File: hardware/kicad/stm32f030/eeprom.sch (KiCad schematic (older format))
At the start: 1 part, among them IC1 AT24CS02-SSHM

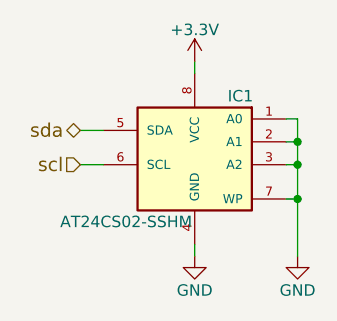
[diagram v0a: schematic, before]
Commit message: hardware/kicad/stm32f030: changed i2c bus and eeprom voltage to 5V
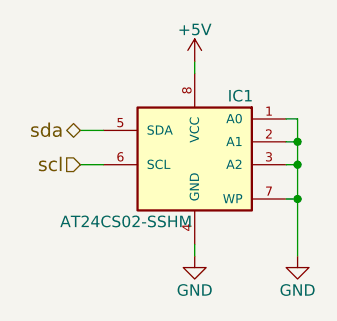
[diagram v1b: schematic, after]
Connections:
- net +3V3 renamed +5V
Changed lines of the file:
@@
 $EndComp
 $Comp
-L +3.3V #PWR045
-U 1 1 589C205E
-P 5600 2850
-F 0 "#PWR045" H 5600 2700 50  0001 C CNN
-F 1 "+3.3V" H 5600 2990 50  0000 C CNN
-F 2 "" H 5600 2850 50  0000 C CNN
-F 3 "" H 5600 2850 50  0000 C CNN
-	1    5600 2850
-	1    0    0    -1
-$EndComp
-$Comp
-L GND #PWR046
+L GND #PWR045
 U 1 1 589C2085
 P 5600 3700
-F 0 "#PWR046" H 5600 3450 50  0001 C CNN
+F 0 "#PWR045" H 5600 3450 50  0001 C CNN
 F 1 "GND" H 5600 3550 50  0000 C CNN
 F 2 "" H 5600 3700 50  0000 C CNN
@@
 	6050 3300 6000 3300
 $Comp
-L GND #PWR047
+L GND #PWR046
 U 1 1 589C239F
 P 6050 3700
-F 0 "#PWR047" H 6050 3450 50  0001 C CNN
+F 0 "#PWR046" H 6050 3450 50  0001 C CNN
 F 1 "GND" H 6050 3550 50  0000 C CNN
 F 2 "" H 6050 3700 50  0000 C CNN
@@
 Wire Wire Line
 	5600 2900 5600 2850
+$Comp
+L +5V #PWR047
+U 1 1 58BC2D81
+P 5600 2850
+F 0 "#PWR047" H 5600 2700 50  0001 C CNN
+F 1 "+5V" H 5600 2990 50  0000 C CNN
+F 2 "" H 5600 2850 50  0001 C CNN
+F 3 "" H 5600 2850 50  0001 C CNN
+	1    5600 2850
+	1    0    0    -1
+$EndComp
 $EndSCHEMATC
